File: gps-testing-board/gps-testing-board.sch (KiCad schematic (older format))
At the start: 14 parts

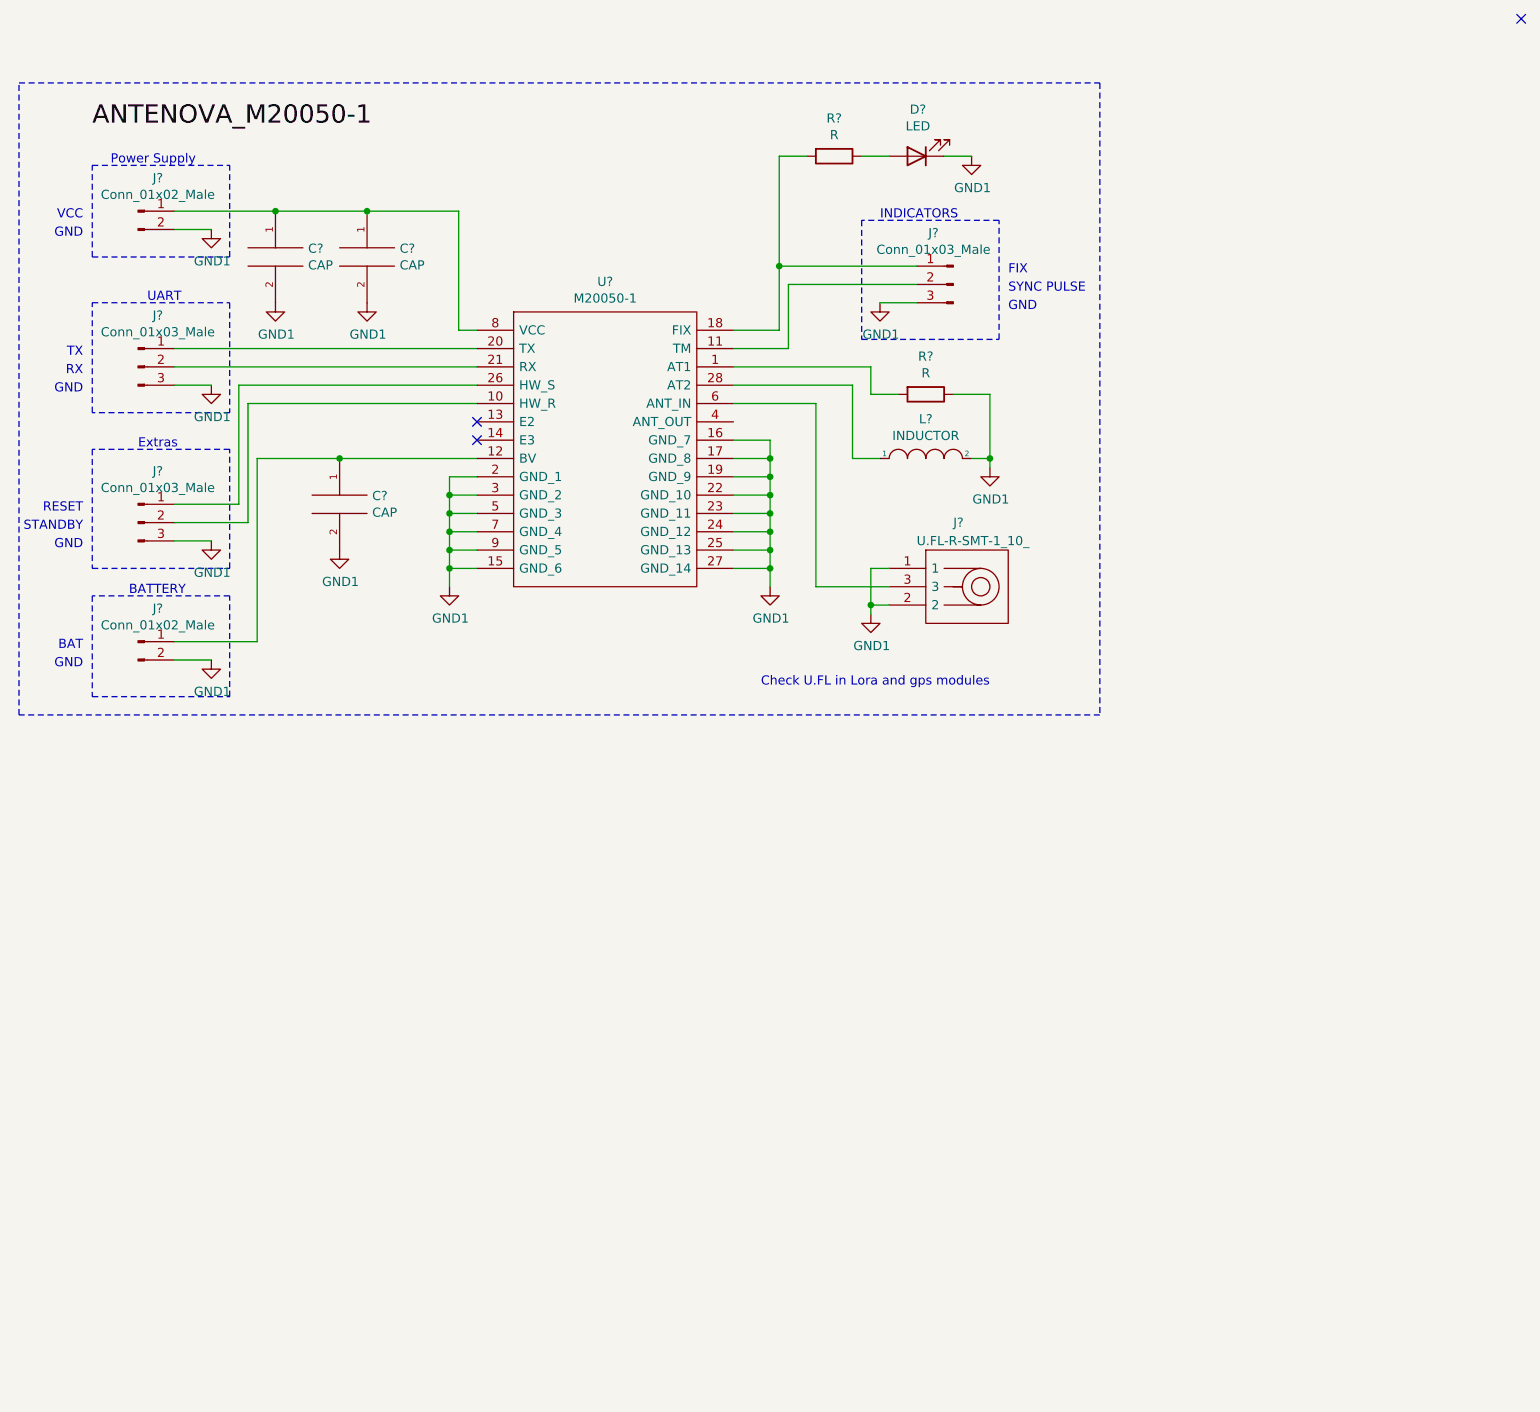
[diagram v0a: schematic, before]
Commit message: Added PCB and battery holders
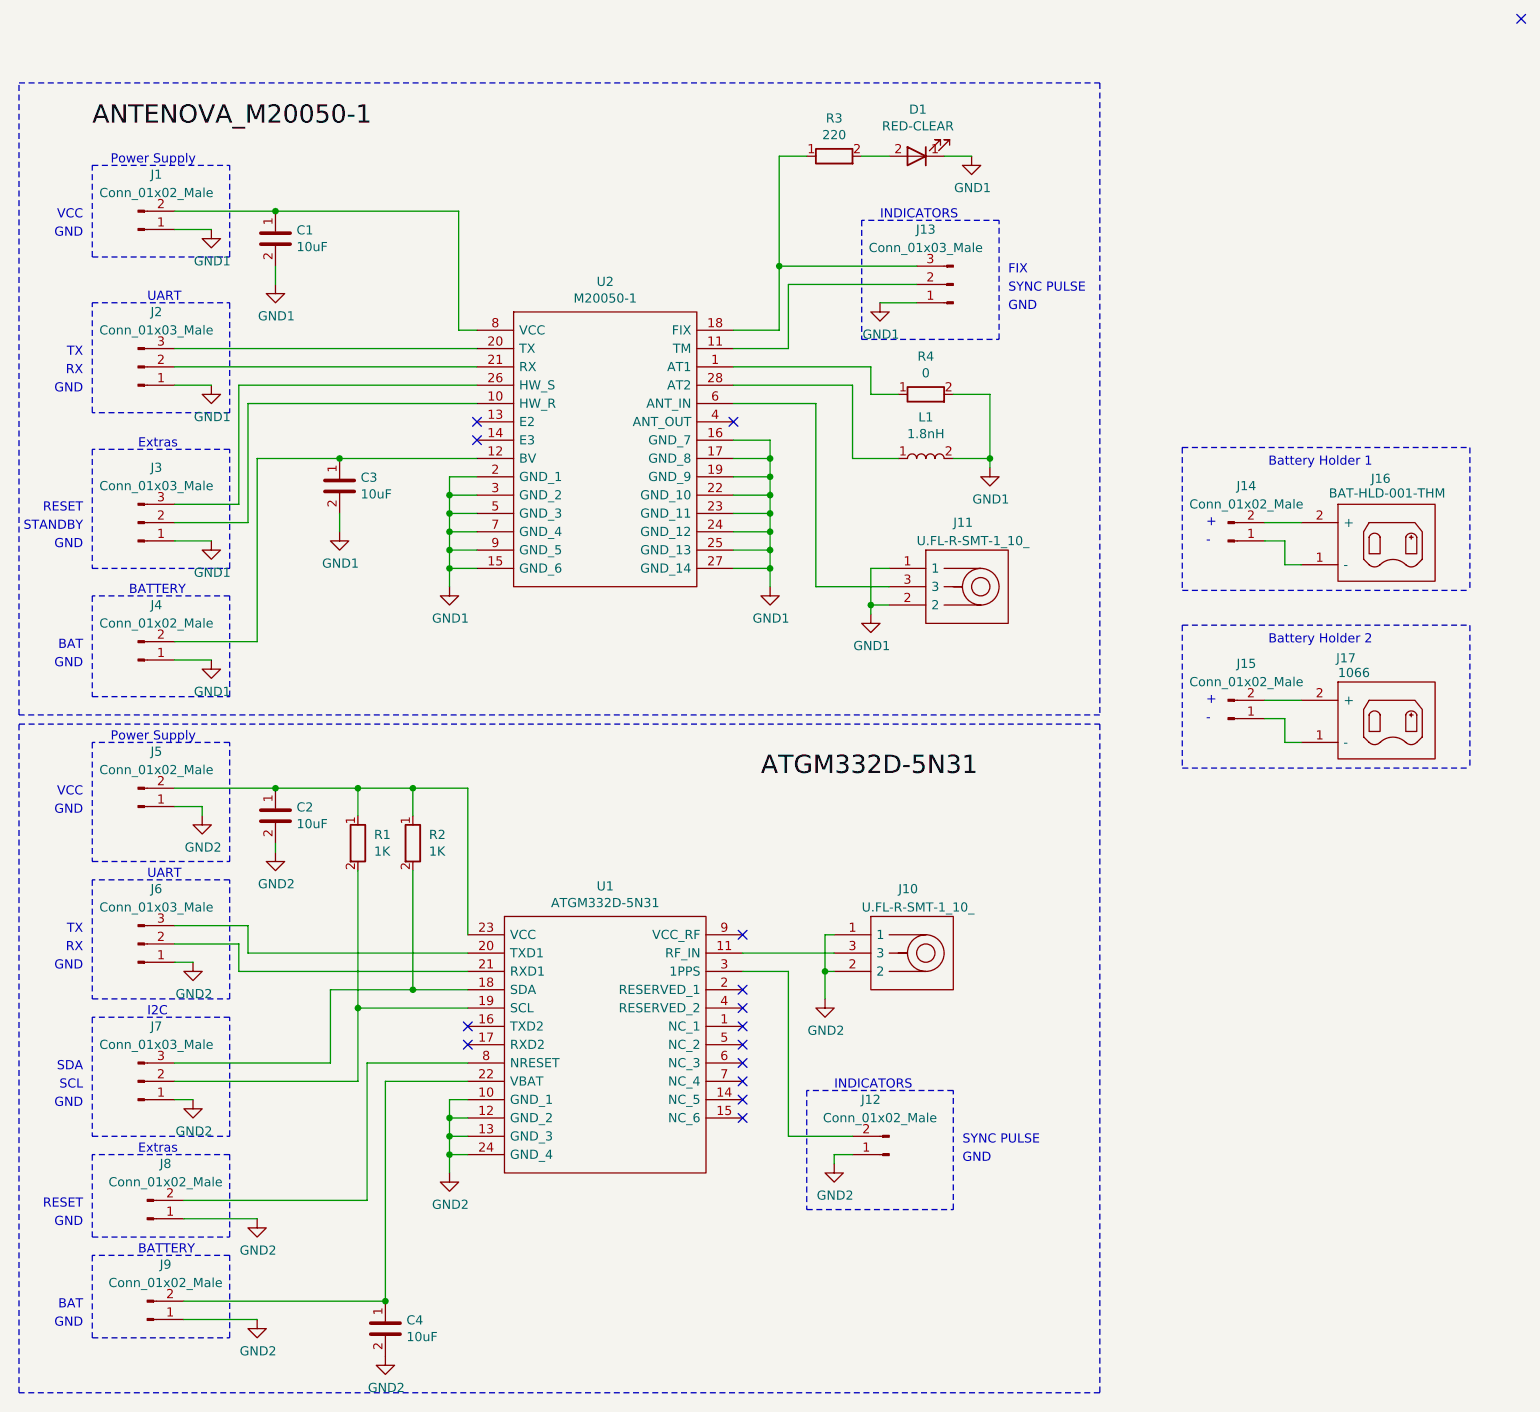
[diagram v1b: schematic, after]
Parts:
- removed C? (x3): CAP, symbol pspice:CAP
- removed D?: LED, symbol Device:LED
- removed L?: INDUCTOR, symbol pspice:INDUCTOR
- removed R? (x2): R, symbol Device:R
- added C1, C2, C3, C4: 10uF, Capacitor_SMD:C_0805_2012Metric, symbol C-10uF-0805:10uF
- added D1: RED-CLEAR, LED_SMD:LED_0805_2012Metric, symbol LED-RED-CLEAR-0805:RED-CLEAR
- added J10: U.FL-R-SMT-1_10_, U.FL-R-SMT-1(10):U.FL-R-SMT-1_10_, symbol U.FL-R-SMT-1_10_:U.FL-R-SMT-1_10_
- added J12, J14, J15, J5, J8, J9: Conn_01x02_Male, Connector_PinSocket_2.54mm:PinSocket_1x02_P2.54mm_Vertical, symbol Connector:Conn_01x02_Male
- added J16: BAT-HLD-001-THM, BAT-HLD-001-THM:BATHLD001THM, symbol BAT-HLD-001-THM:BAT-HLD-001-THM
- added J17: 1066, BAT-1066:BAT-1066, symbol BAT-1066:1066
- added J6, J7: Conn_01x03_Male, Connector_PinSocket_2.54mm:PinSocket_1x03_P2.54mm_Vertical, symbol Connector:Conn_01x03_Male
- added L1: 1.8nH, Inductor_SMD:L_0805_2012Metric, symbol L-1.8nH-0805:1.8nH
- added R1, R2: 1K, Resistor_SMD:R_0805_2012Metric, symbol R-1K-0805:1K
- added R3: 220, Resistor_SMD:R_0805_2012Metric, symbol R-220-0805:220
- added R4: 0, Resistor_SMD:R_0805_2012Metric, symbol R-0-0805:0
- added U1: ATGM332D-5N31, ATGM332D-5N31:ATGM332D5N31, symbol ATGM332D-5N31:ATGM332D-5N31
- J1, J4: renamed from J?; footprint (none) -> Connector_PinSocket_2.54mm:PinSocket_1x02_P2.54mm_Vertical
- J11: renamed from J?; footprint U.FL-R-SMT-1(10) -> U.FL-R-SMT-1(10):U.FL-R-SMT-1_10_; Manufacturer Name (none) -> Hirose; Manufacturer Part Number (none) -> U.FL-R-SMT-1(10); Supplier 1 (none) -> Digi-Key; Supplier 2 (none) -> Mouser; Supplier Part Number 1 (none) -> H11891CT-ND; Supplier Part Number 2 (none) -> 798-U.FL-R-SMT-110
- J13, J2, J3: renamed from J?; footprint (none) -> Connector_PinSocket_2.54mm:PinSocket_1x03_P2.54mm_Vertical
- U2: renamed from U?; footprint M200501 -> M20050-1:M200501
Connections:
- net GND1: now also J1.1 (Pin_1), J13.1 (Pin_1), J2.1 (Pin_1), J3.1 (Pin_1), J4.1 (Pin_1), C1.2, C3.2, D1.1 (K), L1.2, R4.2; no longer J1.2 (Pin_2), J13.3 (Pin_3), J2.3 (Pin_3), J3.3 (Pin_3), J4.2 (Pin_2)
- net at U2.1 (AT1): now also R4.1
- net at U2.12 (BV): now also J4.2 (Pin_2), C3.1; no longer J4.1 (Pin_1)
- net at U2.18 (FIX): now also J13.3 (Pin_3), R3.1; no longer J13.1 (Pin_1)
- net at U2.20 (TX): now also J2.3 (Pin_3); no longer J2.1 (Pin_1)
- net at U2.26 (HW_S): now also J3.3 (Pin_3); no longer J3.1 (Pin_1)
- net at U2.28 (AT2): now also L1.1
- net at U2.8 (VCC): now also J1.2 (Pin_2), C1.1; no longer J1.1 (Pin_1)
- new net: J10.3, U1.11 (RF_IN)
- new net: J7.3 (Pin_3), R2.2, U1.18 (SDA)
- new net: J7.2 (Pin_2), R1.2, U1.19 (SCL)
- new net: J6.3 (Pin_3), U1.20 (TXD1)
- new net: J6.2 (Pin_2), U1.21 (RXD1)
- new net: C4.1, J9.2 (Pin_2), U1.22 (VBAT)
- new net: C2.1, J5.2 (Pin_2), R1.1, R2.1, U1.23 (VCC)
- new net: J12.2 (Pin_2), U1.3 (1PPS)
- new net: J8.2 (Pin_2), U1.8 (NRESET)
- new net: D1.2 (A), R3.2
- new net: J14.1 (Pin_1), J16.1 (-)
- new net: J14.2 (Pin_2), J16.2 (+)
- new net: J15.1 (Pin_1), J17.1 (-)
- new net: J15.2 (Pin_2), J17.2 (+)
- new net GND2: C2.2, C4.2, J10.1, J10.2, J12.1 (Pin_1), J5.1 (Pin_1), J6.1 (Pin_1), J7.1 (Pin_1), J8.1 (Pin_1), J9.1 (Pin_1), U1.10 (GND_1), U1.12 (GND_2), U1.13 (GND_3), U1.24 (GND_4)
- no-connect marks 3 -> 15
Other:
- note added: "+"
- note added: "-"
- note added: "Battery Holder 1"
- note added: "Battery Holder 2"
- note added: "I2C"
- note added: "SCL"
- note added: "SDA"
- note removed: "Check U.FL in Lora and gps modules"
